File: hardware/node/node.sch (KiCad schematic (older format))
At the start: 64 parts, among them J1 BOOT0_Jumper, J2 FTDI, J3 SMA Female, J4 2 x AA, J5 SWD, Q1 Si2323DDS, SW1 DTSM-65R-V-B, U1 RFM69HW, U2 SHTC3, U3 AT25DF512C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

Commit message: Changed to 22u bul caps
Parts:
- C15, C5: value 100u -> 22u; footprint Capacitor_SMD:CP_Elec_6.3x5.3 -> Capacitor_SMD:CP_Elec_5x5.3; Part SC1C107M6L005VR -> (none); TME Link https://www.tme.eu/se/en/details/sc1c107m6l005vr/85degc-smd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 -> https://www.tme.eu/se/en/details/sc1e226m05005vr/85degc-smd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; TME Price 0.35458 -> 0.36794
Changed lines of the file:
@@
 P 3100 7050
 F 0 "C15" H 3150 7150 50  0000 L CNN
-F 1 "100u" H 3150 6950 50  0000 L CNN
-F 2 "Capacitor_SMD:CP_Elec_6.3x5.3" H 3100 7050 50  0001 C CNN
+F 1 "22u" H 3150 6950 50  0000 L CNN
+F 2 "Capacitor_SMD:CP_Elec_5x5.3" H 3100 7050 50  0001 C CNN
 F 3 "~" H 3100 7050 50  0001 C CNN
-F 4 "SC1C107M6L005VR" H 3100 7050 50  0001 C CNN "Part"
-F 5 "https://www.tme.eu/se/en/details/sc1c107m6l005vr/85degc-smd-electrolytic-capacitors/samwha/" H 0   0   50  0001 C CNN "TME Link"
-F 6 "0.35458" H 0   0   50  0001 C CNN "TME Price"
+F 4 "" H 3100 7050 50  0001 C CNN "Part"
+F 5 "https://www.tme.eu/se/en/details/sc1e226m05005vr/85degc-smd-electrolytic-capacitors/samwha/" H 0   0   50  0001 C CNN "TME Link"
+F 6 "0.36794" H 0   0   50  0001 C CNN "TME Price"
 	1    3100 7050
 	-1   0    0    -1
@@
 P 4100 1150
 F 0 "C5" H 4150 1250 50  0000 L CNN
-F 1 "100u" H 4150 1050 50  0000 L CNN
-F 2 "Capacitor_SMD:CP_Elec_6.3x5.3" H 4100 1150 50  0001 C CNN
+F 1 "22u" H 4150 1050 50  0000 L CNN
+F 2 "Capacitor_SMD:CP_Elec_5x5.3" H 4100 1150 50  0001 C CNN
 F 3 "~" H 4100 1150 50  0001 C CNN
-F 4 "SC1C107M6L005VR" H 4100 1150 50  0001 C CNN "Part"
-F 5 "https://www.tme.eu/se/en/details/sc1c107m6l005vr/85degc-smd-electrolytic-capacitors/samwha/" H 0   0   50  0001 C CNN "TME Link"
-F 6 "0.35458" H 0   0   50  0001 C CNN "TME Price"
+F 4 "https://www.tme.eu/se/en/details/sc1e226m05005vr/85degc-smd-electrolytic-capacitors/samwha/" H 0   0   50  0001 C CNN "TME Link"
+F 5 "0.36794" H 0   0   50  0001 C CNN "TME Price"
 	1    4100 1150
 	1    0    0    -1

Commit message: Improved mounting holes and planes
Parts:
- H1, H2, H3, H4: footprint MountingHole:MountingHole_3.2mm_M3 -> humidity:MountingHole_3.2mm_M3
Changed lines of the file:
@@
 F 0 "H1" H 10500 4146 50  0000 L CNN
 F 1 "MountingHole M3" H 10500 4055 50  0000 L CNN
-F 2 "MountingHole:MountingHole_3.2mm_M3" H 10400 4100 50  0001 C CNN
+F 2 "humidity:MountingHole_3.2mm_M3" H 10400 4100 50  0001 C CNN
 F 3 "~" H 10400 4100 50  0001 C CNN
 F 4 "-" H 0   0   50  0001 C CNN "TME Link"
@@
 F 0 "H2" H 10500 4346 50  0000 L CNN
 F 1 "MountingHole M3" H 10500 4255 50  0000 L CNN
-F 2 "MountingHole:MountingHole_3.2mm_M3" H 10400 4300 50  0001 C CNN
+F 2 "humidity:MountingHole_3.2mm_M3" H 10400 4300 50  0001 C CNN
 F 3 "~" H 10400 4300 50  0001 C CNN
 F 4 "-" H 0   0   50  0001 C CNN "TME Link"
@@
 F 0 "H3" H 10500 4546 50  0000 L CNN
 F 1 "MountingHole M3" H 10500 4455 50  0000 L CNN
-F 2 "MountingHole:MountingHole_3.2mm_M3" H 10400 4500 50  0001 C CNN
+F 2 "humidity:MountingHole_3.2mm_M3" H 10400 4500 50  0001 C CNN
 F 3 "~" H 10400 4500 50  0001 C CNN
 F 4 "-" H 0   0   50  0001 C CNN "TME Link"
@@
 F 0 "H4" H 10500 4746 50  0000 L CNN
 F 1 "MountingHole M3" H 10500 4655 50  0000 L CNN
-F 2 "MountingHole:MountingHole_3.2mm_M3" H 10400 4700 50  0001 C CNN
+F 2 "humidity:MountingHole_3.2mm_M3" H 10400 4700 50  0001 C CNN
 F 3 "~" H 10400 4700 50  0001 C CNN
 F 4 "-" H 0   0   50  0001 C CNN "TME Link"

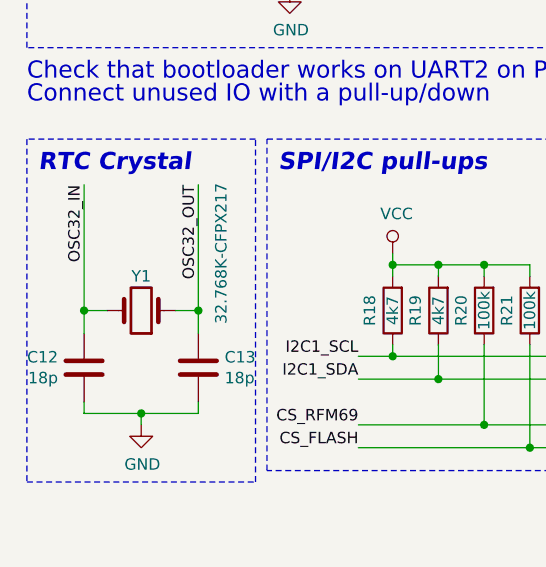
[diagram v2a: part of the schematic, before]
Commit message: DS1307 and PTH crystal
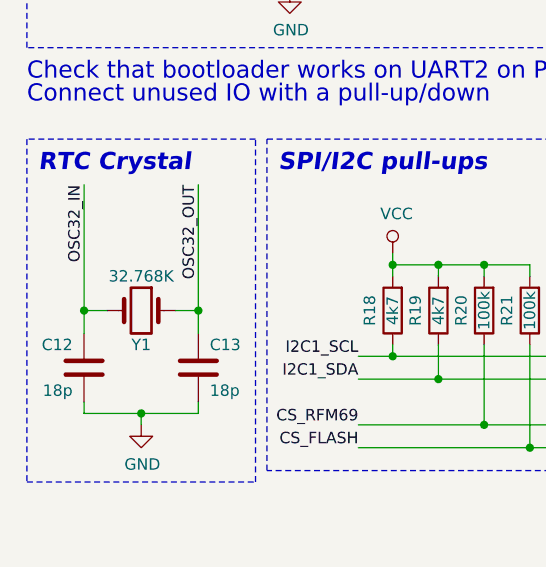
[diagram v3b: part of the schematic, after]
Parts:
- J1: footprint Connector_PinHeader_2.54mm:PinHeader_1x02_P2.54mm_Vertical -> Connector_PinHeader_2.54mm:PinHeader_1x02_P2.54mm_Horizontal
- Y1: value 32.768K-CFPX217 -> 32.768K; footprint humidity:IQD_CFPX-217 -> Crystal:Crystal_C26-LF_D2.1mm_L6.5mm_Horizontal; Part 32.768K-CFPX217 -> (none); TME Link https://www.tme.eu/se/en/details/32.768k-cfpx217/smd-quartz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 -> https://www.tme.eu/se/en/details/26-hx5f-32.768k/tht-quartz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; TME Price 3.42863 -> 1.52097
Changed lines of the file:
@@
 P 1000 4950
 F 0 "Y1" H 1000 4800 50  0000 C CNN
-F 1 "32.768K-CFPX217" V 650 4700 50  0000 C CNN
-F 2 "humidity:IQD_CFPX-217" H 1000 4950 50  0001 C CNN
-F 3 "https://www.tme.eu/Document/cb9f4587d37439d0355f90ad313873e6/cfpx-217.pdf" H 1000 4950 50  0001 C CNN
-F 4 "32.768K-CFPX217" H 1000 4950 50  0001 C CNN "Part"
-F 5 "https://www.tme.eu/se/en/details/32.768k-cfpx217/smd-quartz-crystals/iqd-frequency-products/lfxtal009678/" H 0   0   50  0001 C CNN "TME Link"
-F 6 "3.42863" H 0   0   50  0001 C CNN "TME Price"
+F 1 "32.768K" H 1000 5100 50  0000 C CNN
+F 2 "Crystal:Crystal_C26-LF_D2.1mm_L6.5mm_Horizontal" H 1000 4950 50  0001 C CNN
+F 3 "" H 1000 4950 50  0001 C CNN
+F 4 "https://www.tme.eu/se/en/details/26-hx5f-32.768k/tht-quartz-crystals/ilsi/26-hx5f12-5-32-768khz/" H 1000 4950 50  0001 C CNN "TME Link"
+F 5 "1.52097" H 1000 4950 50  0001 C CNN "TME Price"
 	1    1000 4950
-	-1   0    0    1
+	-1   0    0    -1
 $EndComp
 $Comp
@@
 U 1 1 5CD87672
 P 750 5200
-F 0 "C12" H 636 5154 50  0000 R CNN
-F 1 "18p" H 636 5245 50  0000 R CNN
+F 0 "C12" H 700 5100 50  0000 R CNN
+F 1 "18p" H 700 5300 50  0000 R CNN
 F 2 "Capacitor_SMD:C_0603_1608Metric_Pad1.05x0.95mm_HandSolder" H 788 5050 50  0001 C CNN
 F 3 "~" H 750 5200 50  0001 C CNN
@@
 U 1 1 5CD878C7
 P 1250 5200
-F 0 "C13" H 1365 5246 50  0000 L CNN
-F 1 "18p" H 1365 5155 50  0000 L CNN
+F 0 "C13" H 1300 5300 50  0000 L CNN
+F 1 "18p" H 1300 5100 50  0000 L CNN
 F 2 "Capacitor_SMD:C_0603_1608Metric_Pad1.05x0.95mm_HandSolder" H 1288 5050 50  0001 C CNN
 F 3 "~" H 1250 5200 50  0001 C CNN
@@
 F 0 "J1" H 10750 1350 50  0000 R CNN
 F 1 "BOOT0_Jumper" V 10550 1200 50  0000 C CNN
-F 2 "Connector_PinHeader_2.54mm:PinHeader_1x02_P2.54mm_Vertical" H 10650 1250 50  0001 C CNN
+F 2 "Connector_PinHeader_2.54mm:PinHeader_1x02_P2.54mm_Horizontal" H 10650 1250 50  0001 C CNN
 F 3 "~" H 10650 1250 50  0001 C CNN
 	1    10650 1250

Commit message: Slight layout adjustments
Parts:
- removed TP1, TP3: TestPoint, TestPoint:TestPoint_THTPad_D1.5mm_Drill0.7mm, symbol Connector:TestPoint
- J1: footprint Connector_PinHeader_2.54mm:PinHeader_1x02_P2.54mm_Horizontal -> Connector_PinHeader_2.54mm:PinHeader_1x02_P2.54mm_Vertical
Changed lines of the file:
@@
 F 0 "J1" H 10750 1350 50  0000 R CNN
 F 1 "BOOT0_Jumper" V 10550 1200 50  0000 C CNN
-F 2 "Connector_PinHeader_2.54mm:PinHeader_1x02_P2.54mm_Horizontal" H 10650 1250 50  0001 C CNN
+F 2 "Connector_PinHeader_2.54mm:PinHeader_1x02_P2.54mm_Vertical" H 10650 1250 50  0001 C CNN
 F 3 "~" H 10650 1250 50  0001 C CNN
 	1    10650 1250
@@
 NoConn ~ 7700 2400
 $Comp
-L Connector:TestPoint TP1
-U 1 1 5D000549
-P 8400 4200
-F 0 "TP1" V 8400 4400 50  0000 L CNN
-F 1 "TestPoint" H 8458 4229 50  0001 L CNN
-F 2 "TestPoint:TestPoint_THTPad_D1.5mm_Drill0.7mm" H 8600 4200 50  0001 C CNN
-F 3 "~" H 8600 4200 50  0001 C CNN
-F 4 "-" H 0   0   50  0001 C CNN "TME Link"
-	1    8400 4200
-	0    1    1    0
-$EndComp
-$Comp
-L Connector:TestPoint TP3
-U 1 1 5D0114C3
-P 8400 4350
-F 0 "TP3" V 8400 4550 50  0000 L CNN
-F 1 "TestPoint" H 8458 4379 50  0001 L CNN
-F 2 "TestPoint:TestPoint_THTPad_D1.5mm_Drill0.7mm" H 8600 4350 50  0001 C CNN
-F 3 "~" H 8600 4350 50  0001 C CNN
-F 4 "-" H 0   0   50  0001 C CNN "TME Link"
-	1    8400 4350
-	0    1    1    0
-$EndComp
-$Comp
 L Connector:TestPoint TP2
 U 1 1 5D0333AA
@@
 	0    1    1    0
 $EndComp
-Text Label 7800 4200 0    50   ~ 0
-V_BAT
-Wire Wire Line
-	8400 4200 7800 4200
 $Comp
 L power:GND #PWR0101
@@
 Wire Wire Line
 	7650 5900 8300 5900
-Text Label 7800 4350 0    50   ~ 0
-V_BAT_MID
-Wire Wire Line
-	8400 4350 7800 4350
 $Comp
 L power:VCC #PWR0102

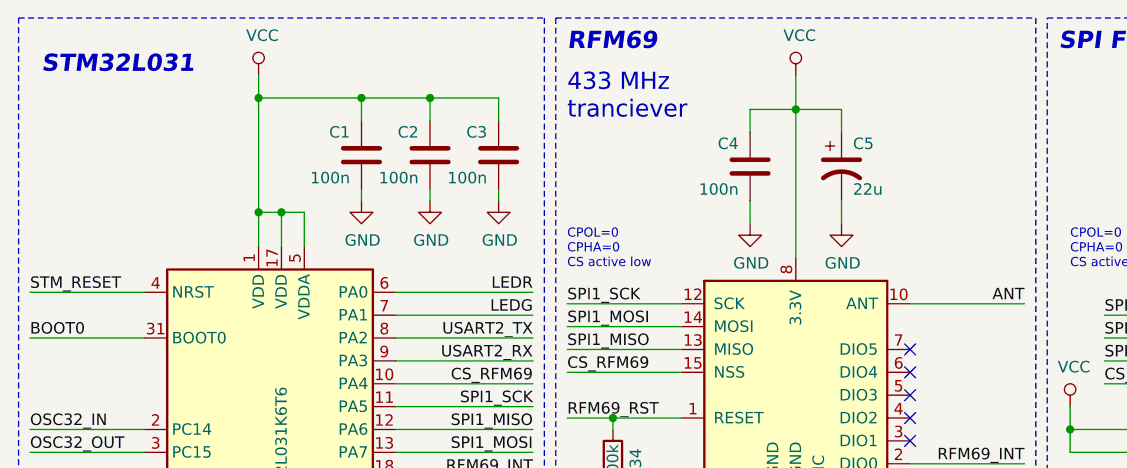
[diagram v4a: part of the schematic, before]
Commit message: Added extra decoupling
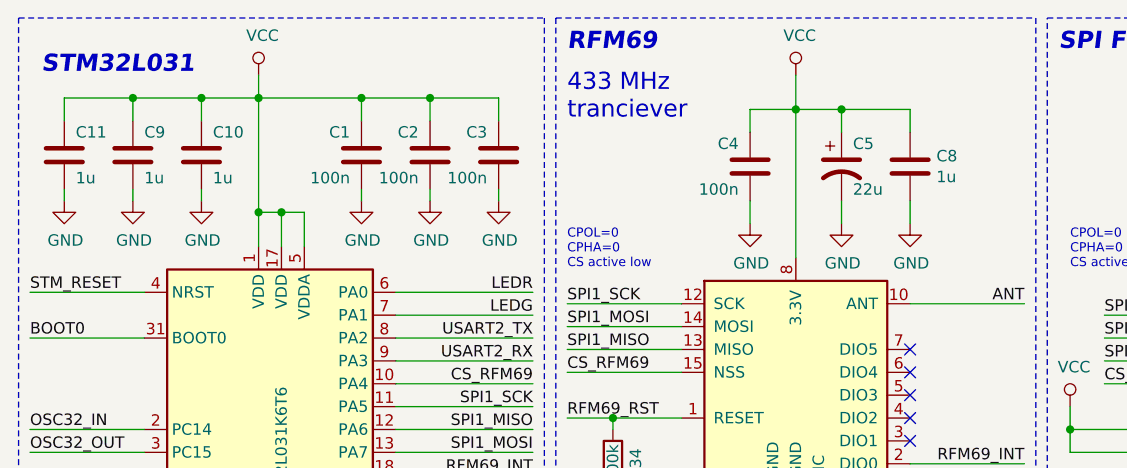
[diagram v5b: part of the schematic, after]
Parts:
- added C10, C11, C8, C9: 1u, Capacitor_SMD:C_0805_2012Metric_Pad1.15x1.40mm_HandSolder, symbol Device:C
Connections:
- net GND: now also C10.2, C11.2, C8.2, C9.2
- net VCC: now also C10.1, C11.1, C8.1, C9.1
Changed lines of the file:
@@
 Wire Wire Line
 	9000 1850 9000 2050
+$Comp
+L Device:C C8
+U 1 1 5D148847
+P 4400 1150
+F 0 "C8" H 4515 1196 50  0000 L CNN
+F 1 "1u" H 4515 1105 50  0000 L CNN
+F 2 "Capacitor_SMD:C_0805_2012Metric_Pad1.15x1.40mm_HandSolder" H 4438 1000 50  0001 C CNN
+F 3 "~" H 4400 1150 50  0001 C CNN
+	1    4400 1150
+	1    0    0    -1
+$EndComp
+Wire Wire Line
+	4100 900  4400 900
+Wire Wire Line
+	4400 900  4400 1000
+Connection ~ 4100 900
+$Comp
+L power:GND #PWR04
+U 1 1 5D157DE7
+P 4400 1400
+F 0 "#PWR04" H 4400 1150 50  0001 C CNN
+F 1 "GND" H 4405 1227 50  0000 C CNN
+F 2 "" H 4400 1400 50  0001 C CNN
+F 3 "" H 4400 1400 50  0001 C CNN
+	1    4400 1400
+	1    0    0    -1
+$EndComp
+Wire Wire Line
+	4400 1300 4400 1400
+$Comp
+L Device:C C10
+U 1 1 5D167AF0
+P 1300 1100
+F 0 "C10" H 1350 1200 50  0000 L CNN
+F 1 "1u" H 1350 1000 50  0000 L CNN
+F 2 "Capacitor_SMD:C_0805_2012Metric_Pad1.15x1.40mm_HandSolder" H 1338 950 50  0001 C CNN
+F 3 "~" H 1300 1100 50  0001 C CNN
+	1    1300 1100
+	1    0    0    -1
+$EndComp
+Wire Wire Line
+	1550 850  1300 850
+Wire Wire Line
+	1300 850  1300 950
+$Comp
+L power:GND #PWR021
+U 1 1 5D1777ED
+P 1300 1300
+F 0 "#PWR021" H 1300 1050 50  0001 C CNN
+F 1 "GND" H 1305 1127 50  0000 C CNN
+F 2 "" H 1300 1300 50  0001 C CNN
+F 3 "" H 1300 1300 50  0001 C CNN
+	1    1300 1300
+	1    0    0    -1
+$EndComp
+Wire Wire Line
+	1300 1250 1300 1300
+$Comp
+L Device:C C9
+U 1 1 5D1878AF
+P 1000 1100
+F 0 "C9" H 1050 1200 50  0000 L CNN
+F 1 "1u" H 1050 1000 50  0000 L CNN
+F 2 "Capacitor_SMD:C_0805_2012Metric_Pad1.15x1.40mm_HandSolder" H 1038 950 50  0001 C CNN
+F 3 "~" H 1000 1100 50  0001 C CNN
+	1    1000 1100
+	1    0    0    -1
+$EndComp
+$Comp
+L power:GND #PWR020
+U 1 1 5D1880F3
+P 1000 1300
+F 0 "#PWR020" H 1000 1050 50  0001 C CNN
+F 1 "GND" H 1005 1127 50  0000 C CNN
+F 2 "" H 1000 1300 50  0001 C CNN
+F 3 "" H 1000 1300 50  0001 C CNN
+	1    1000 1300
+	1    0    0    -1
+$EndComp
+Wire Wire Line
+	1000 1250 1000 1300
+Wire Wire Line
+	1300 850  1000 850
+Wire Wire Line
+	1000 850  1000 950
+Connection ~ 1300 850
+$Comp
+L Device:C C11
+U 1 1 5D20A2C9
+P 700 1100
+F 0 "C11" H 750 1200 50  0000 L CNN
+F 1 "1u" H 750 1000 50  0000 L CNN
+F 2 "Capacitor_SMD:C_0805_2012Metric_Pad1.15x1.40mm_HandSolder" H 738 950 50  0001 C CNN
+F 3 "~" H 700 1100 50  0001 C CNN
+	1    700  1100
+	1    0    0    -1
+$EndComp
+Wire Wire Line
+	1000 850  700  850
+Wire Wire Line
+	700  850  700  950
+Connection ~ 1000 850
+$Comp
+L power:GND #PWR024
+U 1 1 5D21AE99
+P 700 1300
+F 0 "#PWR024" H 700 1050 50  0001 C CNN
+F 1 "GND" H 705 1127 50  0000 C CNN
+F 2 "" H 700 1300 50  0001 C CNN
+F 3 "" H 700 1300 50  0001 C CNN
+	1    700  1300
+	1    0    0    -1
+$EndComp
+Wire Wire Line
+	700  1250 700  1300
 $EndSCHEMATC

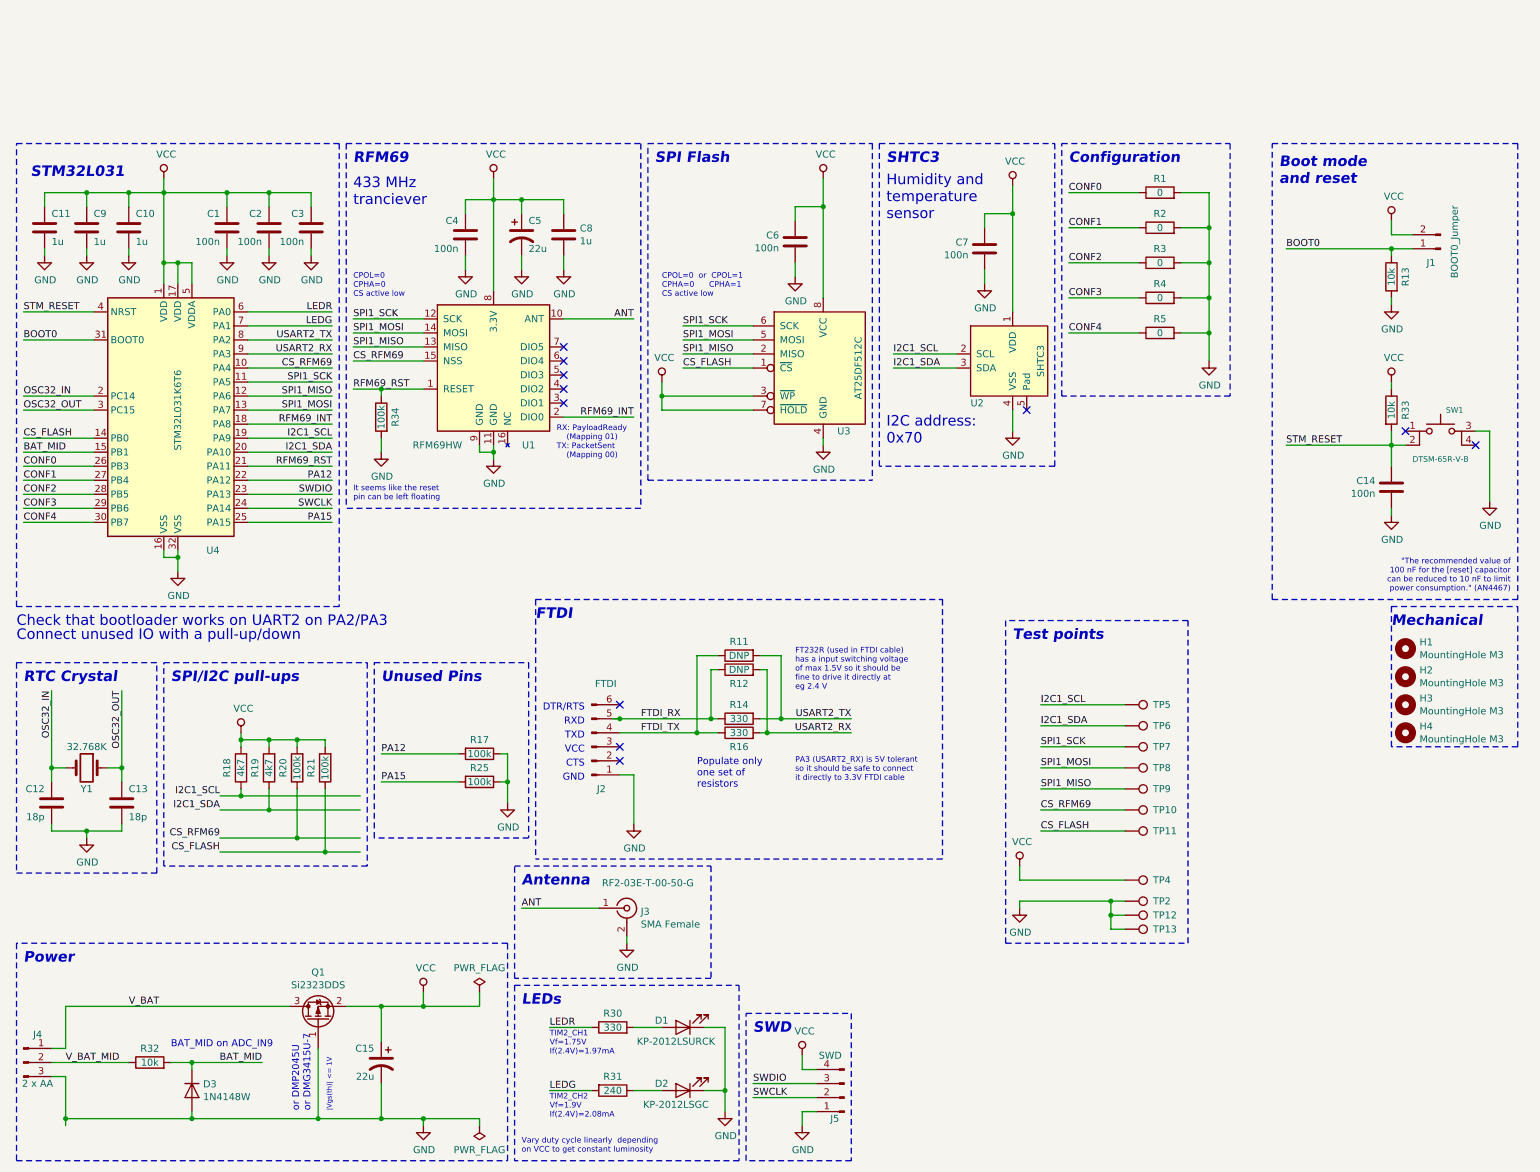
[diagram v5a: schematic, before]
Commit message: Added an extra push button for user input
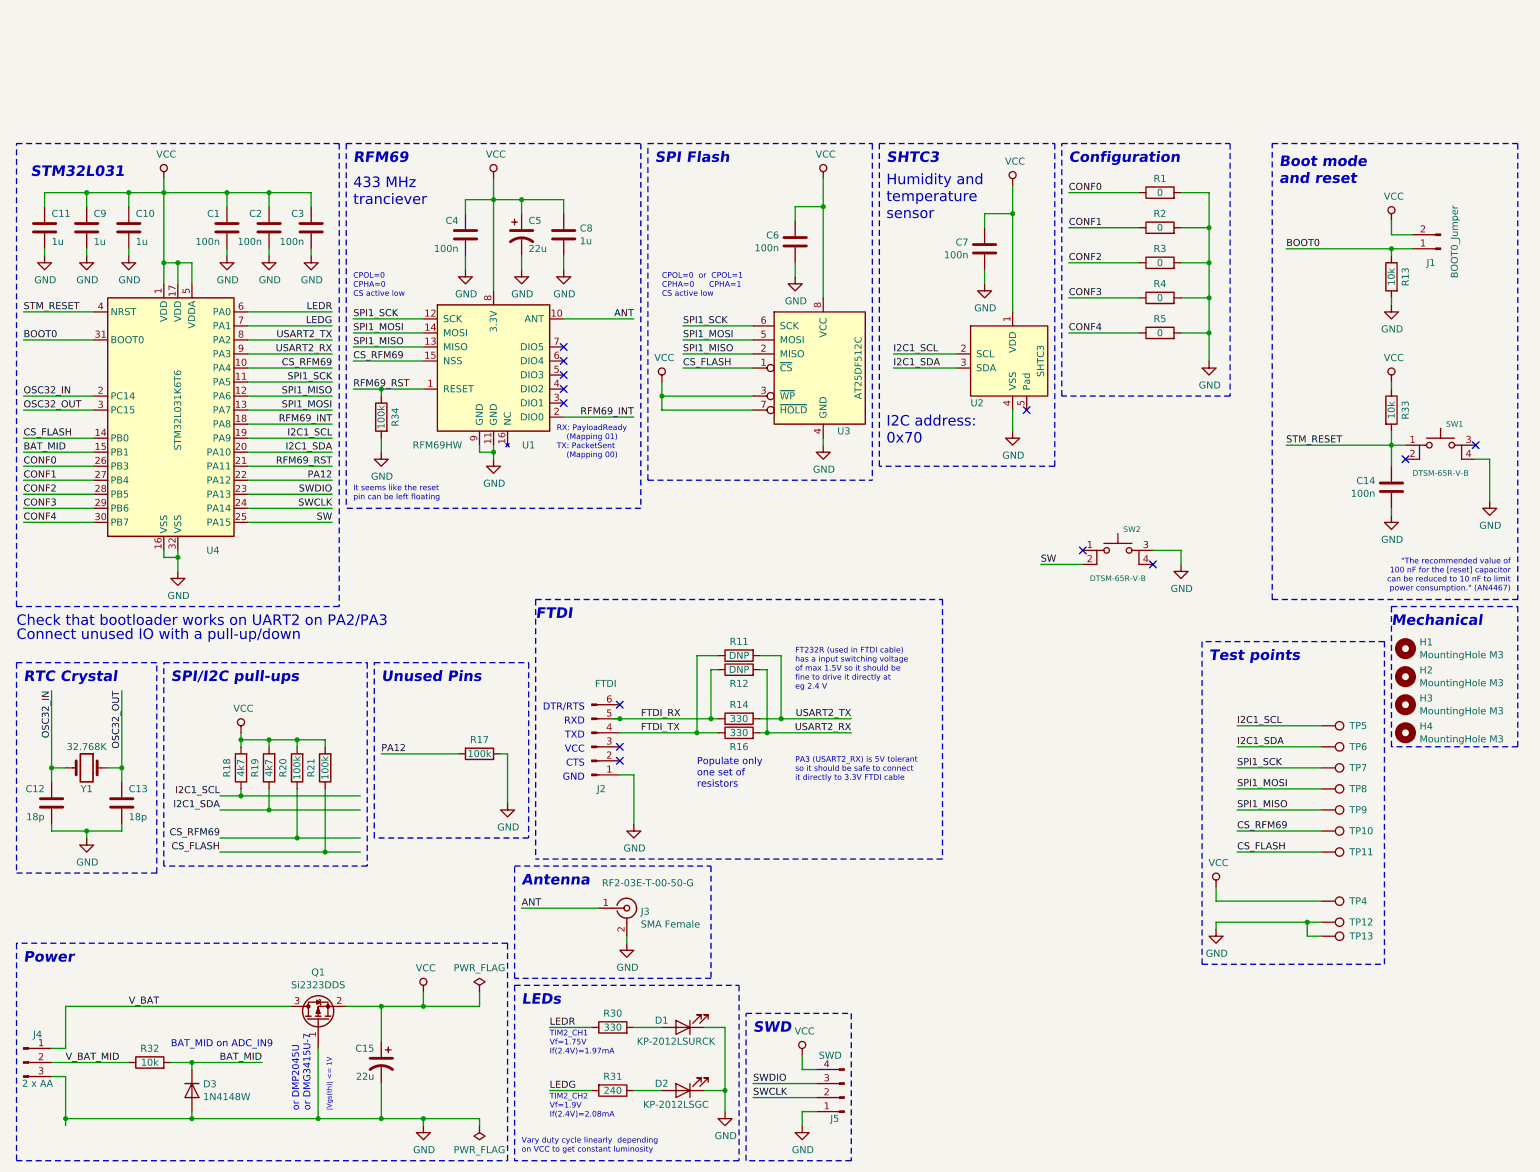
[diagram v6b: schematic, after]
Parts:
- removed R25: 100k, Resistor_SMD:R_0603_1608Metric_Pad1.05x0.95mm_HandSolder, symbol Device:R
- removed TP2: TestPoint, TestPoint:TestPoint_THTPad_1.5x1.5mm_Drill0.7mm, symbol Connector:TestPoint
- added SW2: DTSM-65R-V-B, humidity:SW_SPST_DTSM-6, symbol humidity:SW_Push_4pin
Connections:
- net GND: now also SW1.4, SW2.3; no longer SW1.3
- net STM_RESET: now also SW1.1; no longer SW1.2
- net PA15 renamed SW
- net SW: now also SW2.2
- no-connect marks 11 -> 13
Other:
- moved on the sheet: SW1, TP10, TP11, TP12, TP13, TP4, TP5, TP6, TP7, TP8, TP9
